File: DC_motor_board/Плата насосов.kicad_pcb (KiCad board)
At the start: 2 copper layers, 85 x 65 mm, 158 parts, among them J1 Prog (PinHeader_2x03_P2.54mm), J2 DG142R-5.08-04P-14 IN24V, J3 DG142R-5.08-02P-14 OUT, J4 DG142R-5.08-02P-14 OUT, J5 DebugUSART (PinHeader_01x03_P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, J6 Debug GPIO (PinHeader_01x02_P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, Q1 DTC114ECA (SOT-23), Q2 DTC114ECA (SOT-23), Q3 IRF4905SPbF (D2PAK), Q4 BTN8962TA, Q5 BTN8962TA, Q6 BTN8962TA, Q7 BTN8962TA, U1 ADM3485EARZ-REEL (SOIC-8), U2 pia141M30 (SOIC-16), U3 STM32G070RBTx (LQFP-64), U4 AM1SS-2403SJZ, U5 pia162M30 (SOIC-16), U6 pia162M30 (SOIC-16), U7 L78L05 (SOT89-3)

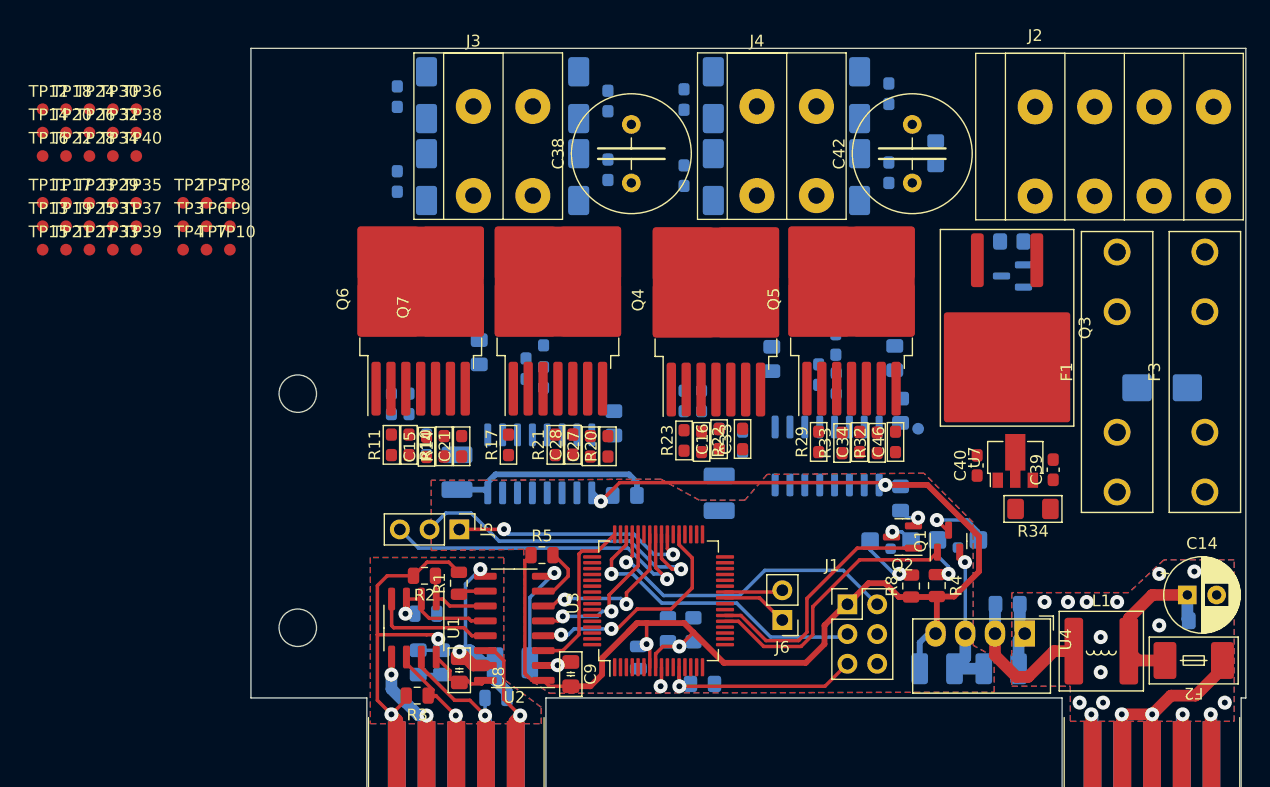
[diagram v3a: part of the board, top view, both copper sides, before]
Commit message: PCB AND SCHEMS DC MOTOR
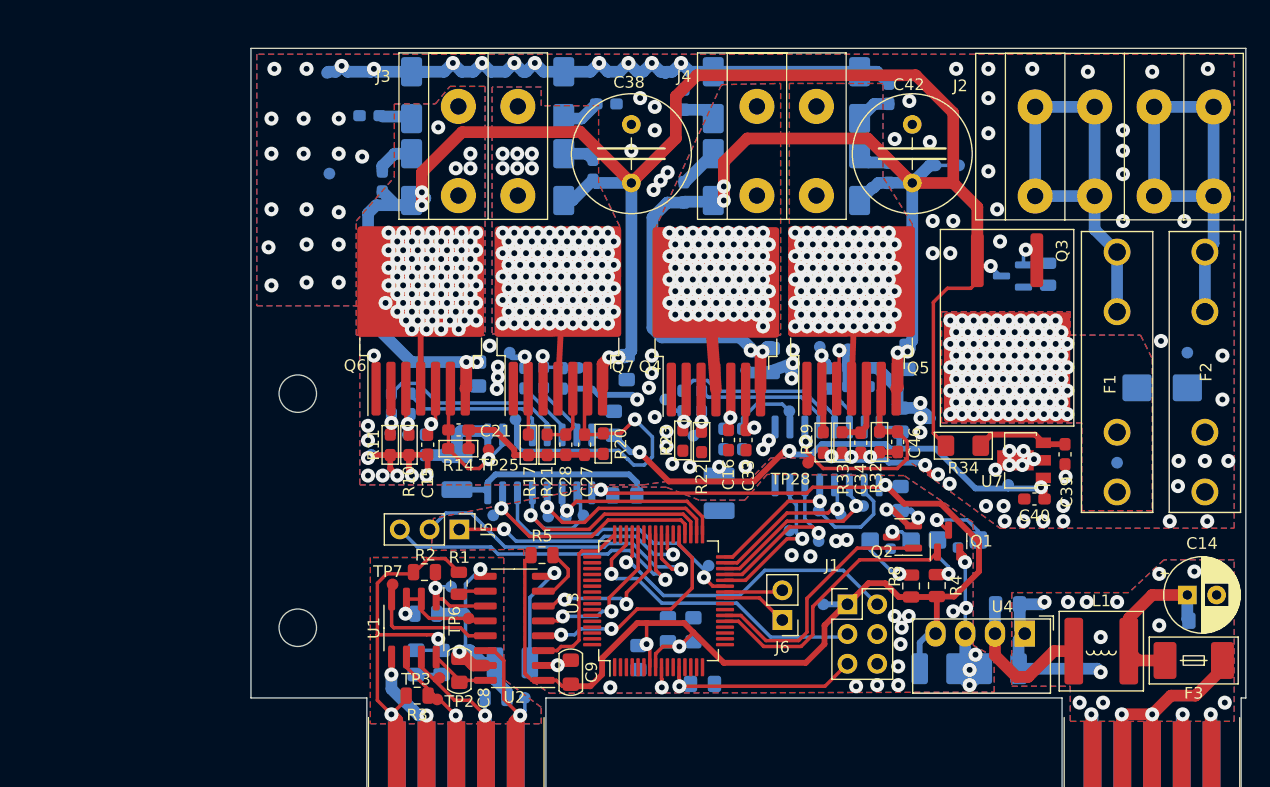
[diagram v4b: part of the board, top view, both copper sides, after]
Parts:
- removed TP35, TP36: TestPoint, PCM_4ms_TestPoint:TestPoint_D1
- C11, C12, C18, C19, C22, C23, C30, C31, C35, C41, C5, C8, C9: footprint PCM_Capacitor_SMD_AKL:C_0805_2012Metric_Pad1.18x1.45mm_HandSolder -> PCM_Capacitor_SMD_AKL:C_0805_2012Metric_Pad1.15x1.40mm
- C15, C16, C28, C34: footprint PCM_Capacitor_SMD_AKL:C_0603_1608Metric_Pad1.08x0.95mm_HandSolder -> Capacitor_SMD:C_0603_1608Metric_Pad1.08x0.95mm_HandSolder
- C17, C20, C21, C24, C25, C27, C29, C32, C33, C36, C37, C46: footprint PCM_Resistor_SMD_AKL:R_0603_1608Metric_Pad1.05x0.95mm_HandSolder -> Capacitor_SMD:C_0603_1608Metric_Pad1.08x0.95mm_HandSolder
- C3: footprint PCM_Capacitor_SMD_Handsoldering_AKL:C_0805_2012Metric_Pad1.15x1.40mm -> PCM_Capacitor_SMD_AKL:C_0805_2012Metric_Pad1.15x1.40mm
- C7: footprint PCM_Capacitor_SMD_AKL:C_0805_2012Metric -> PCM_Capacitor_SMD_AKL:C_0805_2012Metric_Pad1.15x1.40mm
- F2: value 0452.500MRL -> Fuse 5A ZH266 (2 клипсы); footprint PCM_Fuse_Handsoldering_AKL:Fuse_Littelfuse-NANO2-451_453 -> Fuse:Fuseholder_100_series_5x20mm_D1,5
- F3: value Fuse 5A ZH266 (2 клипсы) -> 0452.500MRL; footprint Fuse:Fuseholder_100_series_5x20mm_D1,5 -> PCM_Fuse_Handsoldering_AKL:Fuse_Littelfuse-NANO2-451_453
- R9: footprint PCM_Resistor_SMD_AKL:R_0805_2012Metric_Pad1.20x1.40mm_HandSolder -> PCM_4ms_Resistor:R_0805_2012Metric
- TP10, TP11, TP12, TP13, TP14, TP15, TP16, TP17, TP18, TP19, TP20, TP21, TP22, TP23, TP24, TP26, TP27, TP29, TP30, TP31, TP32, TP33, TP34, TP37, TP38, TP39, TP4, TP40, TP5, TP8, TP9: moved to B.Cu
- moved TP40 91.4 mm to (169.0, 91.5), turned to 180 degrees
- moved TP9 78.4 mm to (163.0, 100.9), turned to 180 degrees
- moved TP14 77.0 mm to (141.3, 104.6), turned to 180 degrees
- moved TP16 74.8 mm to (139.4, 105.4), turned to 180 degrees
- moved TP12 74.6 mm to (137.5, 105.0), turned to 180 degrees
- moved TP18 74.1 mm to (137.5, 107.6), turned to 180 degrees
- moved TP20 70.5 mm to (135.0, 106.7), turned to 180 degrees
- moved TP28 66.8 mm to (136.6, 100.9)
- moved TP30 66.1 mm to (140.0, 91.2), turned to 180 degrees
- moved TP26 64.4 mm to (135.0, 96.5), turned to 180 degrees
- moved TP38 63.9 mm to (141.5, 87.0), turned to 180 degrees
- moved TP32 63.1 mm to (137.6, 91.0), turned to 180 degrees
- moved TP17 63.0 mm to (128.1, 109.7), turned to 180 degrees
- moved TP8 62.4 mm to (149.5, 75.5), turned to 180 degrees
- moved TP10 59.1 mm to (137.9, 113.0), turned to 90 degrees
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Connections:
- F2 pad 1: Net-(RS2-Pin_2) -> GND2
- F2 pad 2: +24V -> Net-(J2-Pin_3)
- F3 pad 1: GND2 -> Net-(RS2-Pin_2)
- F3 pad 2: Net-(J2-Pin_3) -> +24V
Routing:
- net /+24VOUT: track 0.00 -> 240.7 mm, vias 0 -> 13
- net GND2: track 0.00 -> 129.5 mm, vias 0 -> 119
- net Net-(D6-K): track 0.00 -> 49.3 mm, vias 0 -> 73
- net +5V: track 0.00 -> 48.1 mm, vias 0 -> 3
- net Net-(J2-Pin_1): track 0.00 -> 36.1 mm
- net Net-(J2-Pin_3): track 0.00 -> 35.6 mm
- net Net-(Q7-IS): track 0.00 -> 26.4 mm, vias 0 -> 1
- net /Enable_2: track 0.00 -> 25.8 mm, vias 0 -> 1
- net /IS2_2: track 0.00 -> 23.7 mm, vias 0 -> 1
- net /Enable_1: track 0.00 -> 21.6 mm, vias 0 -> 1
- net /IS1_2: track 0.00 -> 20.6 mm, vias 0 -> 1
- net Net-(Q5-IS): track 0.00 -> 20.2 mm, vias 0 -> 1
- net Net-(D10-A): track 0.00 -> 18.9 mm, vias 0 -> 81
- net Net-(D5-K): track 0.00 -> 18.8 mm, vias 0 -> 79
- net Net-(D11-K): track 0.00 -> 17.9 mm, vias 0 -> 96
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- added copper zone on B.Cu, net GND2
- added copper zone on F.Cu, net GND2
- added copper zone on B.Cu, net Net-(D10-A)
- added copper zone on F.Cu, net Net-(D10-A)
- added copper zone on B.Cu, net Net-(D11-K)
- added copper zone on F.Cu, net Net-(D11-K)
- added copper zone on B.Cu, net Net-(D3-A1)
- added copper zone on F.Cu, net Net-(D3-A1)
- added copper zone on B.Cu, net Net-(D5-K)
- added copper zone on F.Cu, net Net-(D5-K)
- added copper zone on B.Cu, net Net-(D6-K)
- added copper zone on F.Cu, net Net-(D6-K)
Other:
- board text added: "+"
- board text added: "-"

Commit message: RENEW ALL BOARDS
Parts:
- moved R6 2.73 mm to (107.8, 119.3), turned to -90 degrees
- moved R3 0.55 mm to (103.0, 120.3)
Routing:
- net GND1: track 37.1 -> 40.3 mm
- net /+24VOUT: track 240.7 -> 237.9 mm
- net Net-(RS1-Pin_4): track 18.1 -> 19.5 mm
- net Net-(RS1-Pin_3): track 16.6 -> 15.4 mm
- removed copper zone on F.Cu, net Net-(D10-A)
- removed copper zone on F.Cu, net Net-(D6-K)

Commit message: fix "pia" typo
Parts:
- U2: value pia141M30 (SOIC-16) -> PAI141M30 (SOIC-16)
- U5, U6: value pia162M30 (SOIC-16) -> PAI162M30 (SOIC-16)
